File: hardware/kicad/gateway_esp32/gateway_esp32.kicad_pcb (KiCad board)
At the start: 2 copper layers, 60 x 32 mm, 4 parts, among them J1 PinHeader_1x02_P2.54mm_Vertic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, SW1 SW_PUSH_6mm, U1 PinHeader_2x19_P2.54mm_Vertic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

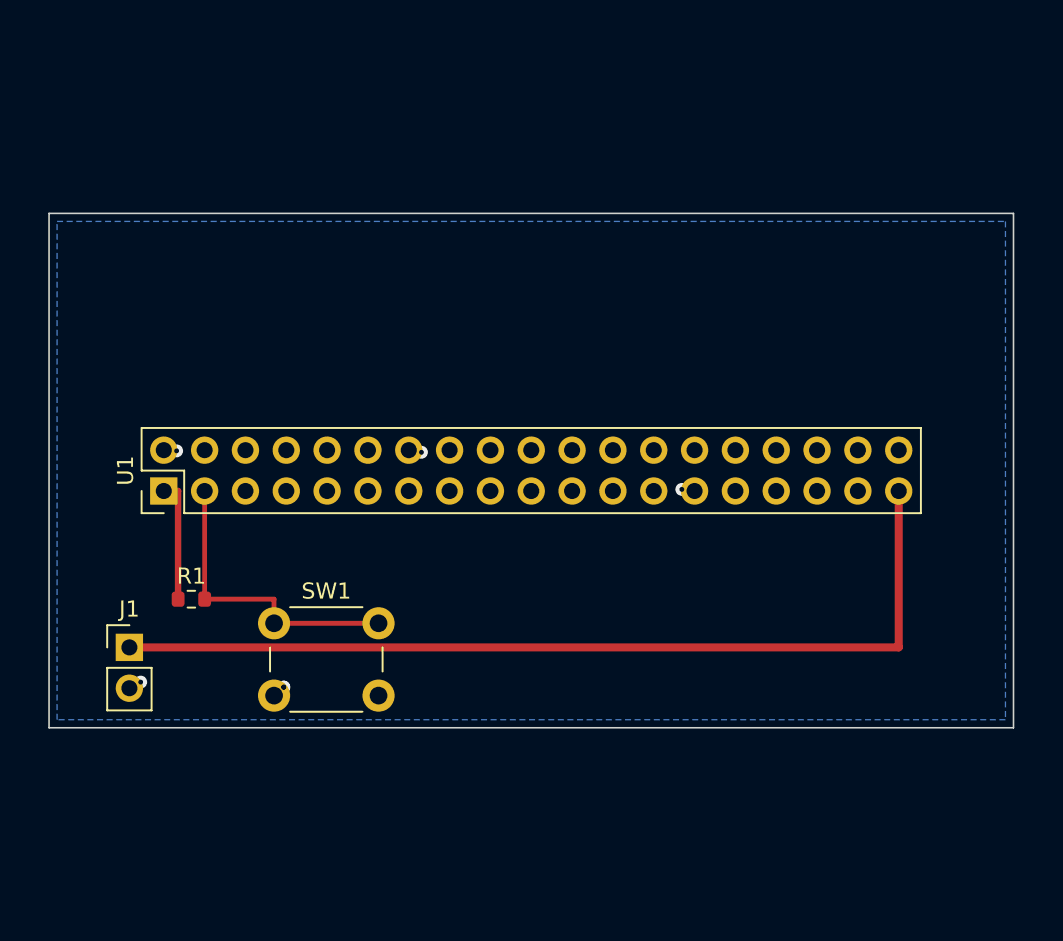
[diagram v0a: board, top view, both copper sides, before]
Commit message: Layouts finish, BM832A migration, fab package, quote, docs and status report
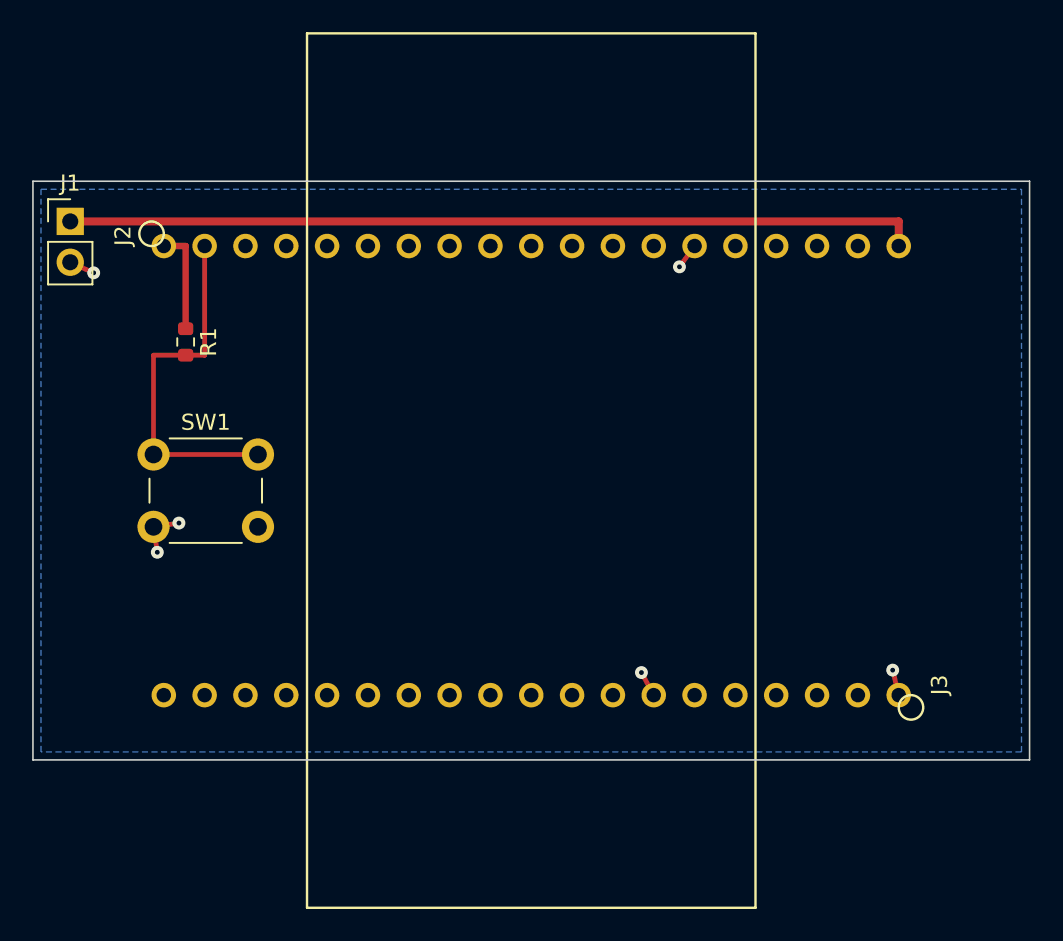
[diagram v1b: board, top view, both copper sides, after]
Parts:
- U1: value PinHeader_2x19_P2.54mm_Vertical -> ESP32-DevKitC-32E; footprint PinHeader_2x19_P2.54mm_Vertical -> ESP32-DevKitC-32E_Carrier
- moved J1 26.8 mm to (71.3, 84.5)
- moved U1 22.9 mm to (100.0, 100.0), turned to -90 degrees
- moved R1 16.0 mm to (78.5, 92.0), turned to -90 degrees
- moved SW1 12.9 mm to (76.5, 99.0)
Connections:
- U1 pad 19: (no net) -> +5V
- U1 pad 2: GND -> EN
- U1 pad 20: (no net) -> GND
- U1 pad 26: (no net) -> GND
- U1 pad 27: GND -> (no net)
- U1 pad 3: EN -> (no net)
- U1 pad 37: +5V -> (no net)
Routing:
- net GND: track 4.80 -> 9.60 mm
- net +5V: track 57.6 -> 53.1 mm
- net EN: track 19.0 -> 22.7 mm
- net +3V3: track 7.62 -> 6.50 mm
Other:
- board size 60 x 32 mm -> 62 x 36 mm
